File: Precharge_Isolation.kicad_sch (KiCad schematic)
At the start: 3 parts

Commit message: voltage sensor cleanup
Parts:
- gave numbers to parts that had none: 3
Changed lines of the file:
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@@
 		(dnp no)
 		(fields_autoplaced yes)
-		(property "Reference" "Q?"
+		(property "Reference" "Q4"
 			(at 90.805 38.0999 0)
 			(show_name no)
@@
 			(project "PS-PrechargeBoard"
 				(path "/74d17fe6-68d4-4bd7-954a-e2bbb58b1f1e/5b236d54-dfec-450f-96e4-88b51678f51f"
-					(reference "Q?")
+					(reference "Q3")
 					(unit 1)
 				)
 				(path "/74d17fe6-68d4-4bd7-954a-e2bbb58b1f1e/d5231689-0a25-4774-9952-2a5e507de834"
-					(reference "Q?")
+					(reference "Q4")
 					(unit 1)
 				)
@@
 		(in_pos_files yes)
 		(dnp no)
-		(property "Reference" "K?"
+		(property "Reference" "K2"
 			(at 55.88 25.4 0)
 			(show_name no)
@@
 			(project "PS-PrechargeBoard"
 				(path "/74d17fe6-68d4-4bd7-954a-e2bbb58b1f1e/5b236d54-dfec-450f-96e4-88b51678f51f"
-					(reference "K?")
+					(reference "K1")
 					(unit 1)
 				)
 				(path "/74d17fe6-68d4-4bd7-954a-e2bbb58b1f1e/d5231689-0a25-4774-9952-2a5e507de834"
-					(reference "K?")
+					(reference "K2")
 					(unit 1)
 				)
@@
 		(in_pos_files yes)
 		(dnp no)
-		(property "Reference" "D?"
+		(property "Reference" "D17"
 			(at 35.56 19.05 0)
 			(show_name no)
@@
 			(project "PS-PrechargeBoard"
 				(path "/74d17fe6-68d4-4bd7-954a-e2bbb58b1f1e/5b236d54-dfec-450f-96e4-88b51678f51f"
-					(reference "D?")
+					(reference "D16")
 					(unit 1)
 				)
 				(path "/74d17fe6-68d4-4bd7-954a-e2bbb58b1f1e/d5231689-0a25-4774-9952-2a5e507de834"
-					(reference "D?")
-					(unit 1)
-				)
+					(reference "D17")
+					(unit 1)
+				)

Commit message: updated usb-c connector
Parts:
- renumbered D17 to D4, K2 to K1, Q4 to Q1
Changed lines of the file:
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@@
 		(dnp no)
 		(fields_autoplaced yes)
-		(property "Reference" "Q4"
+		(property "Reference" "Q1"
 			(at 90.805 38.0999 0)
 			(show_name no)
@@
 			(project "PS-PrechargeBoard"
 				(path "/74d17fe6-68d4-4bd7-954a-e2bbb58b1f1e/5b236d54-dfec-450f-96e4-88b51678f51f"
-					(reference "Q3")
+					(reference "Q2")
 					(unit 1)
 				)
 				(path "/74d17fe6-68d4-4bd7-954a-e2bbb58b1f1e/d5231689-0a25-4774-9952-2a5e507de834"
-					(reference "Q4")
+					(reference "Q1")
 					(unit 1)
 				)
@@
 		(in_pos_files yes)
 		(dnp no)
-		(property "Reference" "K2"
+		(property "Reference" "K1"
 			(at 55.88 25.4 0)
 			(show_name no)
@@
 			(project "PS-PrechargeBoard"
 				(path "/74d17fe6-68d4-4bd7-954a-e2bbb58b1f1e/5b236d54-dfec-450f-96e4-88b51678f51f"
+					(reference "K2")
+					(unit 1)
+				)
+				(path "/74d17fe6-68d4-4bd7-954a-e2bbb58b1f1e/d5231689-0a25-4774-9952-2a5e507de834"
 					(reference "K1")
-					(unit 1)
-				)
-				(path "/74d17fe6-68d4-4bd7-954a-e2bbb58b1f1e/d5231689-0a25-4774-9952-2a5e507de834"
-					(reference "K2")
 					(unit 1)
 				)
@@
 		(in_pos_files yes)
 		(dnp no)
-		(property "Reference" "D17"
+		(property "Reference" "D4"
 			(at 35.56 19.05 0)
 			(show_name no)
@@
 			(project "PS-PrechargeBoard"
 				(path "/74d17fe6-68d4-4bd7-954a-e2bbb58b1f1e/5b236d54-dfec-450f-96e4-88b51678f51f"
-					(reference "D16")
+					(reference "D8")
 					(unit 1)
 				)
 				(path "/74d17fe6-68d4-4bd7-954a-e2bbb58b1f1e/d5231689-0a25-4774-9952-2a5e507de834"
-					(reference "D17")
-					(unit 1)
-				)
+					(reference "D4")
+					(unit 1)
+				)

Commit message: footprints & schematic cute-ification
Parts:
- removed D4: VSSAF522-M3/H, UTSVT-Passives:SODFL5026X125N, symbol Device:D_Schottky
- added D4: VSSAF510HM3/H, LHRS_Passives:SODFL5226X100N, symbol lhrs_power:B540C-13-F
- Q1: footprint ActivePrecharge-RevB:RES_PWR263S-35-3300F -> LHRS_ICs:SOT23_NXP
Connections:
- net DRAIN: now also D4.2 (A)
- net VIN_PROT: now also D4.1 (K)
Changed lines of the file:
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@@
+	(wire
+		(pts
+			(xy 29.21 21.59) (xy 31.75 21.59)
+		)
+		(stroke
+			(width 0)
+			(type default)
+		)
+	)
 	(wire
 		(pts
@@
 		(pts
 			(xy 87.63 34.29) (xy 87.63 29.21)
-		)
-		(stroke
-			(width 0)
-			(type default)
-		)
-	)
-	(wire
-		(pts
-			(xy 31.75 21.59) (xy 29.21 21.59)
 		)
 		(stroke
@@
 			)
 		)
-		(property "Footprint" "ActivePrecharge-RevB:RES_PWR263S-35-3300F"
+		(property "Footprint" "LHRS_ICs:SOT23_NXP"
 			(at 90.17 36.83 0)
 			(hide yes)
@@
 				(path "/74d17fe6-68d4-4bd7-954a-e2bbb58b1f1e/d5231689-0a25-4774-9952-2a5e507de834"
 					(reference "Q1")
+					(unit 1)
+				)
+			)
+		)
+	)
+	(symbol
+		(lib_id "lhrs_power:B540C-13-F")
+		(at 35.56 21.59 0)
+		(unit 1)
+		(body_style 1)
+		(exclude_from_sim no)
+		(in_bom yes)
+		(on_board yes)
+		(in_pos_files yes)
+		(dnp no)
+		(property "Reference" "D4"
+			(at 35.56 18.796 0)
+			(show_name no)
+			(do_not_autoplace no)
+			(effects
+				(font
+					(size 1.27 1.27)
+				)
+			)
+		)
+		(property "Value" "VSSAF510HM3/H"
+			(at 35.56 24.384 0)
+			(show_name no)
+			(do_not_autoplace no)
+			(effects
+				(font
+					(size 1.27 1.27)
+				)
+			)
+		)
+		(property "Footprint" "LHRS_Passives:SODFL5226X100N"
+			(at 35.56 21.59 0)
+			(hide yes)
+			(show_name no)
+			(do_not_autoplace no)
+			(effects
+				(font
+					(size 1.27 1.27)
+				)
+			)
+		)
+		(property "Datasheet" "kicad-embed://DIOD-S-A0007810469-1.pdf"
+			(at 35.56 21.59 0)
+			(hide yes)
+			(show_name no)
+			(do_not_autoplace no)
+			(effects
+				(font
+					(size 1.27 1.27)
+				)
+			)
+		)
+		(property "Description" "Diodes Inc B540C-13-F, SMT Schottky Diode, 40V 5A, 2-Pin DO-214AB"
+			(at 35.56 21.59 0)
+			(hide yes)
+			(show_name no)
+			(do_not_autoplace no)
+			(effects
+				(font
+					(size 1.27 1.27)
+				)
+			)
+		)
+		(property "Height" "2.5"
+			(at 35.56 21.59 0)
+			(hide yes)
+			(show_name no)
+			(do_not_autoplace no)
+			(effects
+				(font
+					(size 1.27 1.27)
+				)
+			)
+		)
+		(property "Mouser Part Number" "621-B540C-F"
+			(at 35.56 21.59 0)
+			(hide yes)
+			(show_name no)
+			(do_not_autoplace no)
+			(effects
+				(font
+					(size 1.27 1.27)
+				)
+			)
+		)
+		(property "Mouser Price/Stockl" "https://www.mouser.co.uk/ProductDetail/Diodes-Incorporated/B540C-13-F?qs=v2dnQLbuoRZXHN%2FK4ft5%252Bg%3D%3D"
+			(at 35.56 21.59 0)
+			(hide yes)
+			(show_name no)
+			(do_not_autoplace no)
+			(effects
+				(font
+					(size 1.27 1.27)
+				)
+			)
+		)
+		(property "Manufacturer_Name" "Diodes Incorporated"
+			(at 35.56 21.59 0)
+			(hide yes)
+			(show_name no)
+			(do_not_autoplace no)
+			(effects
+				(font
+					(size 1.27 1.27)
+				)
+			)
+		)
+		(property "Manufacturer_Part_Number" "B540C-13-F"
+			(at 35.56 21.59 0)
+			(hide yes)
+			(show_name no)
+			(do_not_autoplace no)
+			(effects
+				(font
+					(size 1.27 1.27)
+				)
+			)
+		)
+		(pin "1"
+		)
+		(pin "2"
+		)
+		(instances
+			(project "PS-PrechargeBoard"
+				(path "/74d17fe6-68d4-4bd7-954a-e2bbb58b1f1e/5b236d54-dfec-450f-96e4-88b51678f51f"
+					(reference "D8")
+					(unit 1)
+				)
+				(path "/74d17fe6-68d4-4bd7-954a-e2bbb58b1f1e/d5231689-0a25-4774-9952-2a5e507de834"
+					(reference "D4")
 					(unit 1)
 				)
@@
 					(unit 1)
 				)
-			)
-		)
-	)
-	(symbol
-		(lib_id "Device:D_Schottky")
-		(at 35.56 21.59 0)
-		(mirror x)
-		(unit 1)
-		(body_style 1)
-		(exclude_from_sim no)
-		(in_bom yes)
-		(on_board yes)
-		(in_pos_files yes)
-		(dnp no)
-		(property "Reference" "D4"
-			(at 35.56 19.05 0)
-			(show_name no)
-			(do_not_autoplace no)
-			(effects
-				(font
-					(size 1.27 1.27)
-				)
-			)
-		)
-		(property "Value" "VSSAF522-M3/H"
-			(at 35.56 24.13 0)
-			(show_name no)
-			(do_not_autoplace no)
-			(effects
-				(font
-					(size 1.27 1.27)
-				)
-			)
-		)
-		(property "Footprint" "UTSVT-Passives:SODFL5026X125N"
-			(at 35.56 21.59 0)
-			(hide yes)
-			(show_name no)
-			(do_not_autoplace no)
-			(effects
-				(font
-					(size 1.27 1.27)
-				)
-			)
-		)
-		(property "Datasheet" ""
-			(at 35.56 21.59 0)
-			(hide yes)
-			(show_name no)
-			(do_not_autoplace no)
-			(effects
-				(font
-					(size 1.27 1.27)
-				)
-			)
-		)
-		(property "Description" "Flyback diode"
-			(at 35.56 21.59 0)
-			(hide yes)
-			(show_name no)
-			(do_not_autoplace no)
-			(effects
-				(font
-					(size 1.27 1.27)
-				)
-			)
-		)
-		(property "P/N" "VSSAF522-M3/H"
-			(at 35.56 21.59 0)
-			(hide yes)
-			(show_name no)
-			(do_not_autoplace no)
-			(effects
-				(font
-					(size 1.27 1.27)
-				)
-			)
-		)
-		(property "Sim.Device" ""
-			(at 35.56 21.59 90)
-			(hide yes)
-			(show_name no)
-			(do_not_autoplace no)
-			(effects
-				(font
-					(size 1.27 1.27)
-				)
-			)
-		)
-		(property "Sim.Library" ""
-			(at 35.56 21.59 90)
-			(hide yes)
-			(show_name no)
-			(do_not_autoplace no)
-			(effects
-				(font
-					(size 1.27 1.27)
-				)
-			)
-		)
-		(property "Sim.Name" ""
-			(at 35.56 21.59 90)
-			(hide yes)
-			(show_name no)
-			(do_not_autoplace no)
-			(effects
-				(font
-					(size 1.27 1.27)
-				)
-			)
-		)
-		(pin "1"
-		)
-		(pin "2"
-		)
-		(instances
-			(project "PS-PrechargeBoard"
-				(path "/74d17fe6-68d4-4bd7-954a-e2bbb58b1f1e/5b236d54-dfec-450f-96e4-88b51678f51f"
-					(reference "D8")
-					(unit 1)
-				)
-				(path "/74d17fe6-68d4-4bd7-954a-e2bbb58b1f1e/d5231689-0a25-4774-9952-2a5e507de834"
-					(reference "D4")
-					(unit 1)
-				)

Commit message: finished schematic & footprint
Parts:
- K1: footprint LIB_DE1a-12V:DE1a12V -> Precharge_Board:DE1a12V
- Q1: P/N (none) -> IRLML0030TRPBF
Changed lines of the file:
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@@
+			)
+		)
+		(property "P/N" "IRLML0030TRPBF"
+			(at 85.09 39.37 0)
+			(hide yes)
+			(show_name no)
+			(do_not_autoplace no)
+			(effects
+				(font
+					(size 1.27 1.27)
+				)
 			)
 		)
@@
 			)
 		)
-		(property "Footprint" "LIB_DE1a-12V:DE1a12V"
+		(property "Footprint" "Precharge_Board:DE1a12V"
 			(at 74.93 124.13 0)
 			(hide yes)

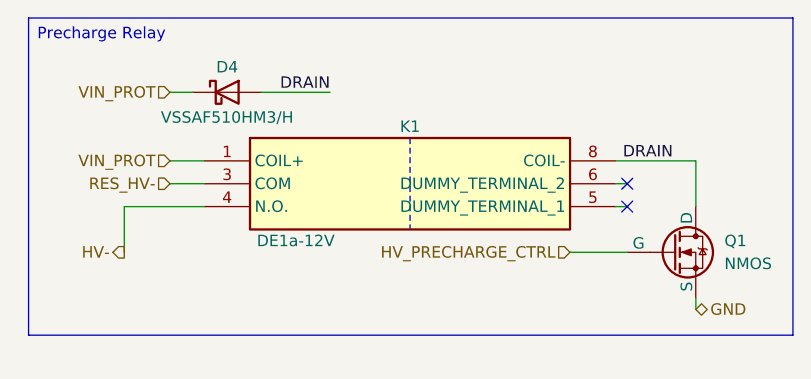
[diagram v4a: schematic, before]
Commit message: 10k ohm resistor to precharge gate
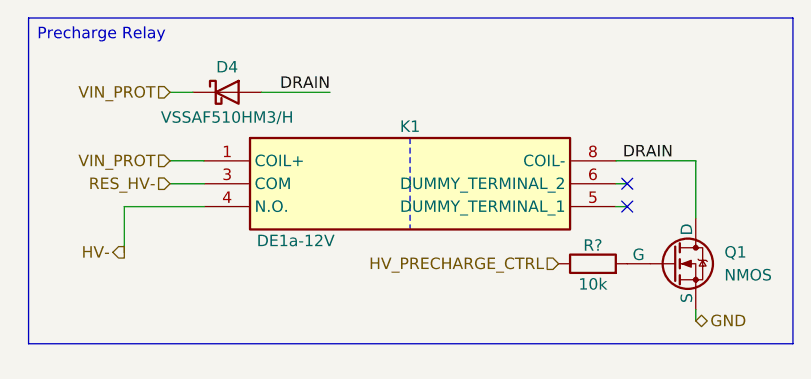
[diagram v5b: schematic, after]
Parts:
- added R?: 10k, symbol Device:R
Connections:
- net HV_PRECHARGE_CTRL: now also R?.1; no longer Q1.2 (G)
- new net: Q1.2 (G), R?.2
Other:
- moved on the sheet: Q1
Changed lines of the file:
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@@
 	(rectangle
 		(start 13.4938 13.3349)
-		(end 98.4249 48.5775)
+		(end 98.4249 49.5299)
 		(stroke
 			(width 0)
@@
 	(wire
 		(pts
-			(xy 87.63 34.29) (xy 87.63 29.21)
+			(xy 87.63 35.56) (xy 87.63 29.21)
 		)
 		(stroke
@@
 	(wire
 		(pts
-			(xy 73.66 39.37) (xy 80.01 39.37)
-		)
-		(stroke
-			(width 0)
-			(type default)
-		)
-	)
-	(wire
-		(pts
 			(xy 24.13 39.37) (xy 24.13 34.29)
 		)
@@
 	(wire
 		(pts
-			(xy 87.63 45.72) (xy 87.63 44.45)
+			(xy 87.63 46.99) (xy 87.63 45.72)
 		)
 		(stroke
@@
 	(hierarchical_label "GND"
 		(shape bidirectional)
-		(at 87.63 45.72 0)
+		(at 87.63 46.99 0)
 		(effects
 			(font
@@
 	(hierarchical_label "HV_PRECHARGE_CTRL"
 		(shape input)
-		(at 73.66 39.37 180)
+		(at 72.39 40.64 180)
 		(effects
 			(font
@@
 	(symbol
 		(lib_id "Simulation_SPICE:NMOS")
-		(at 85.09 39.37 0)
+		(at 85.09 40.64 0)
 		(unit 1)
 		(body_style 1)
@@
 		(fields_autoplaced yes)
 		(property "Reference" "Q1"
-			(at 90.805 38.0999 0)
+			(at 90.805 39.3699 0)
 			(show_name no)
 			(do_not_autoplace no)
@@
 		)
 		(property "Value" "NMOS"
-			(at 90.805 40.6399 0)
+			(at 90.805 41.9099 0)
 			(show_name no)
 			(do_not_autoplace no)
@@
 		)
 		(property "Footprint" "LHRS_ICs:SOT23_NXP"
-			(at 90.17 36.83 0)
+			(at 90.17 38.1 0)
 			(hide yes)
 			(show_name no)
@@
 		)
 		(property "Datasheet" "https://ngspice.sourceforge.io/docs/ngspice-html-manual/manual.xhtml#cha_MOSFETs"
-			(at 85.09 52.07 0)
+			(at 85.09 53.34 0)
 			(hide yes)
 			(show_name no)
@@
 		)
 		(property "Description" "N-MOSFET transistor, drain/source/gate"
-			(at 85.09 39.37 0)
+			(at 85.09 40.64 0)
 			(hide yes)
 			(show_name no)
@@
 		)
 		(property "Sim.Device" "NMOS"
-			(at 85.09 56.515 0)
+			(at 85.09 57.785 0)
 			(hide yes)
 			(show_name no)
@@
 		)
 		(property "Sim.Type" "VDMOS"
-			(at 85.09 58.42 0)
+			(at 85.09 59.69 0)
 			(hide yes)
 			(show_name no)
@@
 		)
 		(property "Sim.Pins" "1=D 2=G 3=S"
-			(at 85.09 54.61 0)
+			(at 85.09 55.88 0)
 			(hide yes)
 			(show_name no)
@@
 		)
 		(property "P/N" "IRLML0030TRPBF"
-			(at 85.09 39.37 0)
+			(at 85.09 40.64 0)
 			(hide yes)
 			(show_name no)
@@
 					(unit 1)
 				)
+			)
+		)
+	)
+	(symbol
+		(lib_id "Device:R")
+		(at 76.2 40.64 90)
+		(unit 1)
+		(body_style 1)
+		(exclude_from_sim no)
+		(in_bom yes)
+		(on_board yes)
+		(in_pos_files yes)
+		(dnp no)
+		(property "Reference" "R?"
+			(at 76.2 38.608 90)
+			(show_name no)
+			(do_not_autoplace no)
+			(effects
+				(font
+					(size 1.27 1.27)
+				)
+			)
+		)
+		(property "Value" "10k"
+			(at 76.2 42.926 90)
+			(show_name no)
+			(do_not_autoplace no)
+			(effects
+				(font
+					(size 1.27 1.27)
+				)
+			)
+		)
+		(property "Footprint" ""
+			(at 76.2 42.418 90)
+			(hide yes)
+			(show_name no)
+			(do_not_autoplace no)
+			(effects
+				(font
+					(size 1.27 1.27)
+				)
+			)
+		)
+		(property "Datasheet" ""
+			(at 76.2 40.64 0)
+			(hide yes)
+			(show_name no)
+			(do_not_autoplace no)
+			(effects
+				(font
+					(size 1.27 1.27)
+				)
+			)
+		)
+		(property "Description" "Resistor"
+			(at 76.2 40.64 0)
+			(hide yes)
+			(show_name no)
+			(do_not_autoplace no)
+			(effects
+				(font
+					(size 1.27 1.27)
+				)
+			)
+		)
+		(pin "2"
+		)
+		(pin "1"
+		)
+		(instances
+			(project "PS-PrechargeBoard"
+				(path "/74d17fe6-68d4-4bd7-954a-e2bbb58b1f1e/5b236d54-dfec-450f-96e4-88b51678f51f"
+					(reference "R?")
+					(unit 1)
+				)
+				(path "/74d17fe6-68d4-4bd7-954a-e2bbb58b1f1e/d5231689-0a25-4774-9952-2a5e507de834"
+					(reference "R?")
+					(unit 1)
+				)

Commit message: updated voltage divider to amc3311
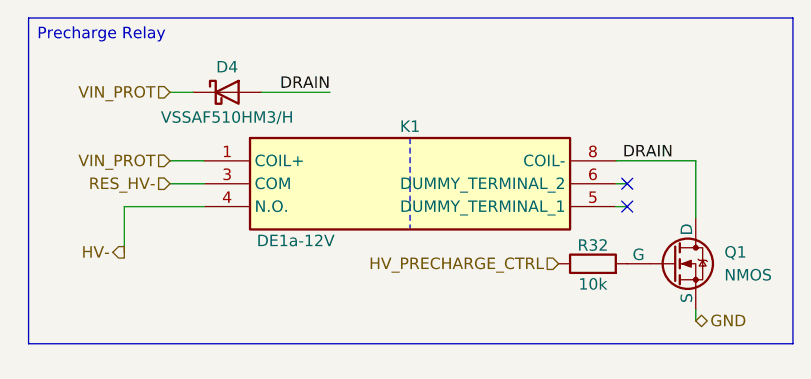
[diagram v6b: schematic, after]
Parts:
- gave numbers to parts that had none: 1
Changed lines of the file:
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@@
 		(in_pos_files yes)
 		(dnp no)
-		(property "Reference" "R?"
+		(property "Reference" "R32"
 			(at 76.2 38.608 90)
 			(show_name no)
@@
 			(project "PS-PrechargeBoard"
 				(path "/74d17fe6-68d4-4bd7-954a-e2bbb58b1f1e/5b236d54-dfec-450f-96e4-88b51678f51f"
-					(reference "R?")
+					(reference "R63")
 					(unit 1)
 				)
 				(path "/74d17fe6-68d4-4bd7-954a-e2bbb58b1f1e/d5231689-0a25-4774-9952-2a5e507de834"
-					(reference "R?")
+					(reference "R32")
 					(unit 1)
 				)

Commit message: fixed hv placement
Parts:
- R32: footprint (none) -> Resistor_SMD:R_0603_1608Metric_Pad0.98x0.95mm_HandSolder
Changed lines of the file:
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@@
 			)
 		)
-		(property "Footprint" ""
+		(property "Footprint" "Resistor_SMD:R_0603_1608Metric_Pad0.98x0.95mm_HandSolder"
 			(at 76.2 42.418 90)
 			(hide yes)

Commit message: restored pp placement
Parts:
- added R5: 10k, Resistor_SMD:R_0603_1608Metric_Pad0.98x0.95mm_HandSolder, symbol Device:R
- R32: value 10k -> 100
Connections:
- net GND: now also R5.1
- net at Q1.2 (G), R32.2: now also R5.2
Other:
- moved on the sheet: R32
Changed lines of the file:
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@@
 	(rectangle
 		(start 13.4938 13.3349)
-		(end 98.4249 49.5299)
+		(end 98.4249 51.4349)
 		(stroke
 			(width 0)
@@
 		)
 	)
+	(junction
+		(at 78.74 40.64)
+		(diameter 0)
+		(color 0 0 0 0)
+	)
 	(no_connect
 		(at 80.01 31.75)
@@
 	(wire
 		(pts
+			(xy 78.74 40.64) (xy 80.01 40.64)
+		)
+		(stroke
+			(width 0)
+			(type default)
+		)
+	)
+	(wire
+		(pts
 			(xy 78.74 34.29) (xy 80.01 34.29)
 		)
@@
 		)
 	)
+	(wire
+		(pts
+			(xy 78.74 49.53) (xy 78.74 48.26)
+		)
+		(stroke
+			(width 0)
+			(type default)
+		)
+	)
+	(wire
+		(pts
+			(xy 77.47 40.64) (xy 78.74 40.64)
+		)
+		(stroke
+			(width 0)
+			(type default)
+		)
+	)
+	(wire
+		(pts
+			(xy 69.85 40.64) (xy 68.58 40.64)
+		)
+		(stroke
+			(width 0)
+			(type default)
+		)
+	)
 	(polyline
 		(pts
@@
 	(wire
 		(pts
-			(xy 87.63 46.99) (xy 87.63 45.72)
+			(xy 87.63 49.53) (xy 87.63 45.72)
 		)
 		(stroke
@@
 	(hierarchical_label "GND"
 		(shape bidirectional)
-		(at 87.63 46.99 0)
+		(at 87.63 49.53 0)
 		(effects
 			(font
@@
 	(hierarchical_label "HV_PRECHARGE_CTRL"
 		(shape input)
-		(at 72.39 40.64 180)
+		(at 68.58 40.64 180)
 		(effects
 			(font
@@
 		)
 	)
+	(hierarchical_label "GND"
+		(shape bidirectional)
+		(at 78.74 49.53 0)
+		(effects
+			(font
+				(size 1.27 1.27)
+			)
+			(justify left)
+		)
+	)
 	(hierarchical_label "RES_HV-"
 		(shape input)
@@
 			)
 			(justify right)
+		)
+	)
+	(symbol
+		(lib_id "Device:R")
+		(at 78.74 44.45 180)
+		(unit 1)
+		(body_style 1)
+		(exclude_from_sim no)
+		(in_bom yes)
+		(on_board yes)
+		(in_pos_files yes)
+		(dnp no)
+		(property "Reference" "R5"
+			(at 81.788 43.688 0)
+			(show_name no)
+			(do_not_autoplace no)
+			(effects
+				(font
+					(size 1.27 1.27)
+				)
+			)
+		)
+		(property "Value" "10k"
+			(at 81.788 45.466 0)
+			(show_name no)
+			(do_not_autoplace no)
+			(effects
+				(font
+					(size 1.27 1.27)
+				)
+			)
+		)
+		(property "Footprint" "Resistor_SMD:R_0603_1608Metric_Pad0.98x0.95mm_HandSolder"
+			(at 80.518 44.45 90)
+			(hide yes)
+			(show_name no)
+			(do_not_autoplace no)
+			(effects
+				(font
+					(size 1.27 1.27)
+				)
+			)
+		)
+		(property "Datasheet" ""
+			(at 78.74 44.45 0)
+			(hide yes)
+			(show_name no)
+			(do_not_autoplace no)
+			(effects
+				(font
+					(size 1.27 1.27)
+				)
+			)
+		)
+		(property "Description" "Resistor"
+			(at 78.74 44.45 0)
+			(hide yes)
+			(show_name no)
+			(do_not_autoplace no)
+			(effects
+				(font
+					(size 1.27 1.27)
+				)
+			)
+		)
+		(pin "2"
+		)
+		(pin "1"
+		)
+		(instances
+			(project "PS-PrechargeBoard"
+				(path "/74d17fe6-68d4-4bd7-954a-e2bbb58b1f1e/5b236d54-dfec-450f-96e4-88b51678f51f"
+					(reference "R36")
+					(unit 1)
+				)
+				(path "/74d17fe6-68d4-4bd7-954a-e2bbb58b1f1e/d5231689-0a25-4774-9952-2a5e507de834"
+					(reference "R5")
+					(unit 1)
+				)
+			)
 		)
 	)
@@
 	(symbol
 		(lib_id "Device:R")
-		(at 76.2 40.64 90)
+		(at 73.66 40.64 90)
 		(unit 1)
 		(body_style 1)
@@
 		(dnp no)
 		(property "Reference" "R32"
-			(at 76.2 38.608 90)
-			(show_name no)
-			(do_not_autoplace no)
-			(effects
-				(font
-					(size 1.27 1.27)
-				)
-			)
-		)
-		(property "Value" "10k"
-			(at 76.2 42.926 90)
+			(at 73.66 38.608 90)
+			(show_name no)
+			(do_not_autoplace no)
+			(effects
+				(font
+					(size 1.27 1.27)
+				)
+			)
+		)
+		(property "Value" "100"
+			(at 73.66 42.926 90)
 			(show_name no)
 			(do_not_autoplace no)
@@
 		)
 		(property "Footprint" "Resistor_SMD:R_0603_1608Metric_Pad0.98x0.95mm_HandSolder"
-			(at 76.2 42.418 90)
+			(at 73.66 42.418 90)
 			(hide yes)
 			(show_name no)
@@
 		)
 		(property "Datasheet" ""
-			(at 76.2 40.64 0)
+			(at 73.66 40.64 0)
 			(hide yes)
 			(show_name no)
@@
 		)
 		(property "Description" "Resistor"
-			(at 76.2 40.64 0)
-			(hide yes)
-			(show_name no)
+			(at 73.66 40.64 0)
+			(hide yes)
+			(show_name no)
